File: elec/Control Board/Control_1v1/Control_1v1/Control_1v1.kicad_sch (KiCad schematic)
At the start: 146 parts, among them J1 DB9_Female_MountingHoles, J10 Conn_02x12_Odd_Even, J11 Screw_Terminal_01x02, J14 Conn_01x10, J2 Conn_01x08, J25 Screw_Terminal_01x02, J26 Conn_01x10, J27 Conn_02x12_Odd_Even, J28 Screw_Terminal_01x02, J29 Conn_01x10, J3 Conn_01x08, J37 Conn_01x04_Pin, J4 Conn_01x08, J5 Conn_01x08, J6 Conn_01x08, J7 Conn_01x10, J8 Conn_02x18_Odd_Even, J9 Conn_01x10, Q601 BSS138

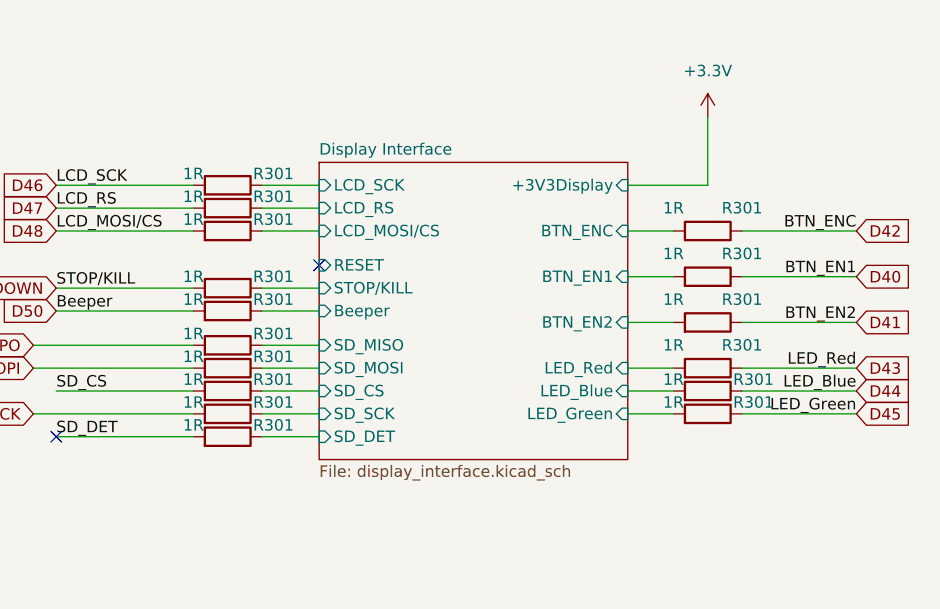
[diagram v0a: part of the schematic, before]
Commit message: unified 1R and 1R0 references
Signed-off-by: lokimetasmith <lokimail@gmail.com>
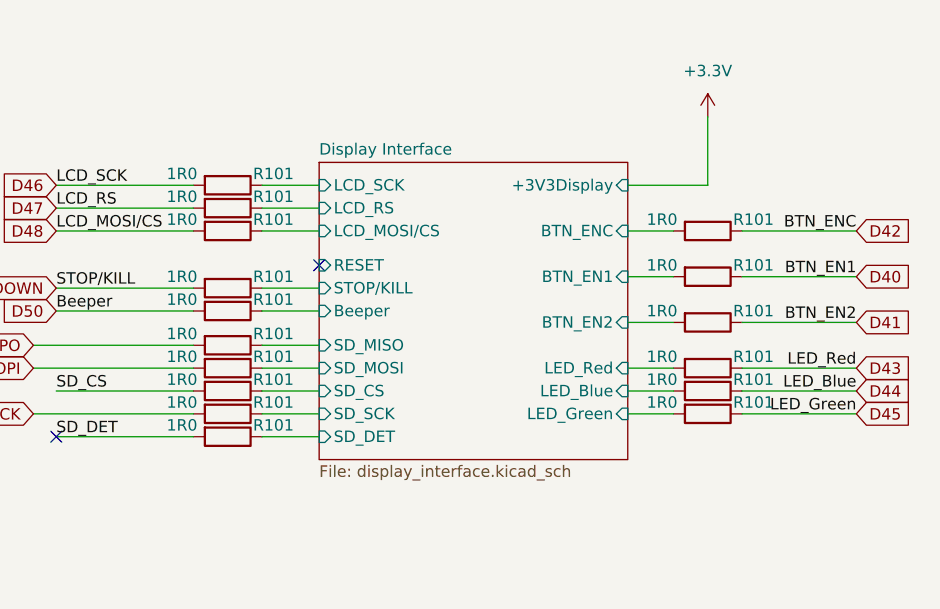
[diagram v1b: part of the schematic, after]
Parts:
- removed R301 (x16): 1R, Resistor_SMD:R_0603_1608Metric_Pad0.98x0.95mm_HandSolder, symbol Device:R
- added R101 (x16): 1R0, Resistor_SMD:R_0603_1608Metric_Pad0.98x0.95mm_HandSolder, symbol Device:R
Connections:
- net CIPO: now also R101.2
- net COPI: now also R101.2
- net D40: now also R101.1
- net D41: now also R101.1
- net D42: now also R101.1
- net D43: now also R101.1
- net D44: now also R101.1
- net D45: now also R101.1
- net D46: now also R101.2
- net D47: now also R101.2
- net D48: now also R101.2
- net D49: now also R101.2
- net D50: now also R101.2
- net Display Interface/BTN_EN1: now also R101.2
- net Display Interface/BTN_EN2: now also R101.2
- net Display Interface/BTN_ENC: now also R101.2
- net Display Interface/Beeper: now also R101.1
- net Display Interface/LCD_MOSI/CS: now also R101.1
- net Display Interface/LCD_RS: now also R101.1
- net Display Interface/LCD_SCK: now also R101.1
- net Display Interface/LED_Blue: now also R101.2
- net Display Interface/LED_Green: now also R101.2
- net Display Interface/LED_Red: now also R101.2
- net Display Interface/SD_CS: now also R101.1
- net Display Interface/SD_DET: now also R101.1
- net Display Interface/SD_MISO: now also R101.1
- net Display Interface/SD_MOSI: now also R101.1
- net Display Interface/SD_SCK: now also R101.1
- net Display Interface/STOP/KILL: now also R101.1
- net SD_CS: now also R101.2
- net SD_DET: now also R101.2
- net SPI_SCK: now also R101.2

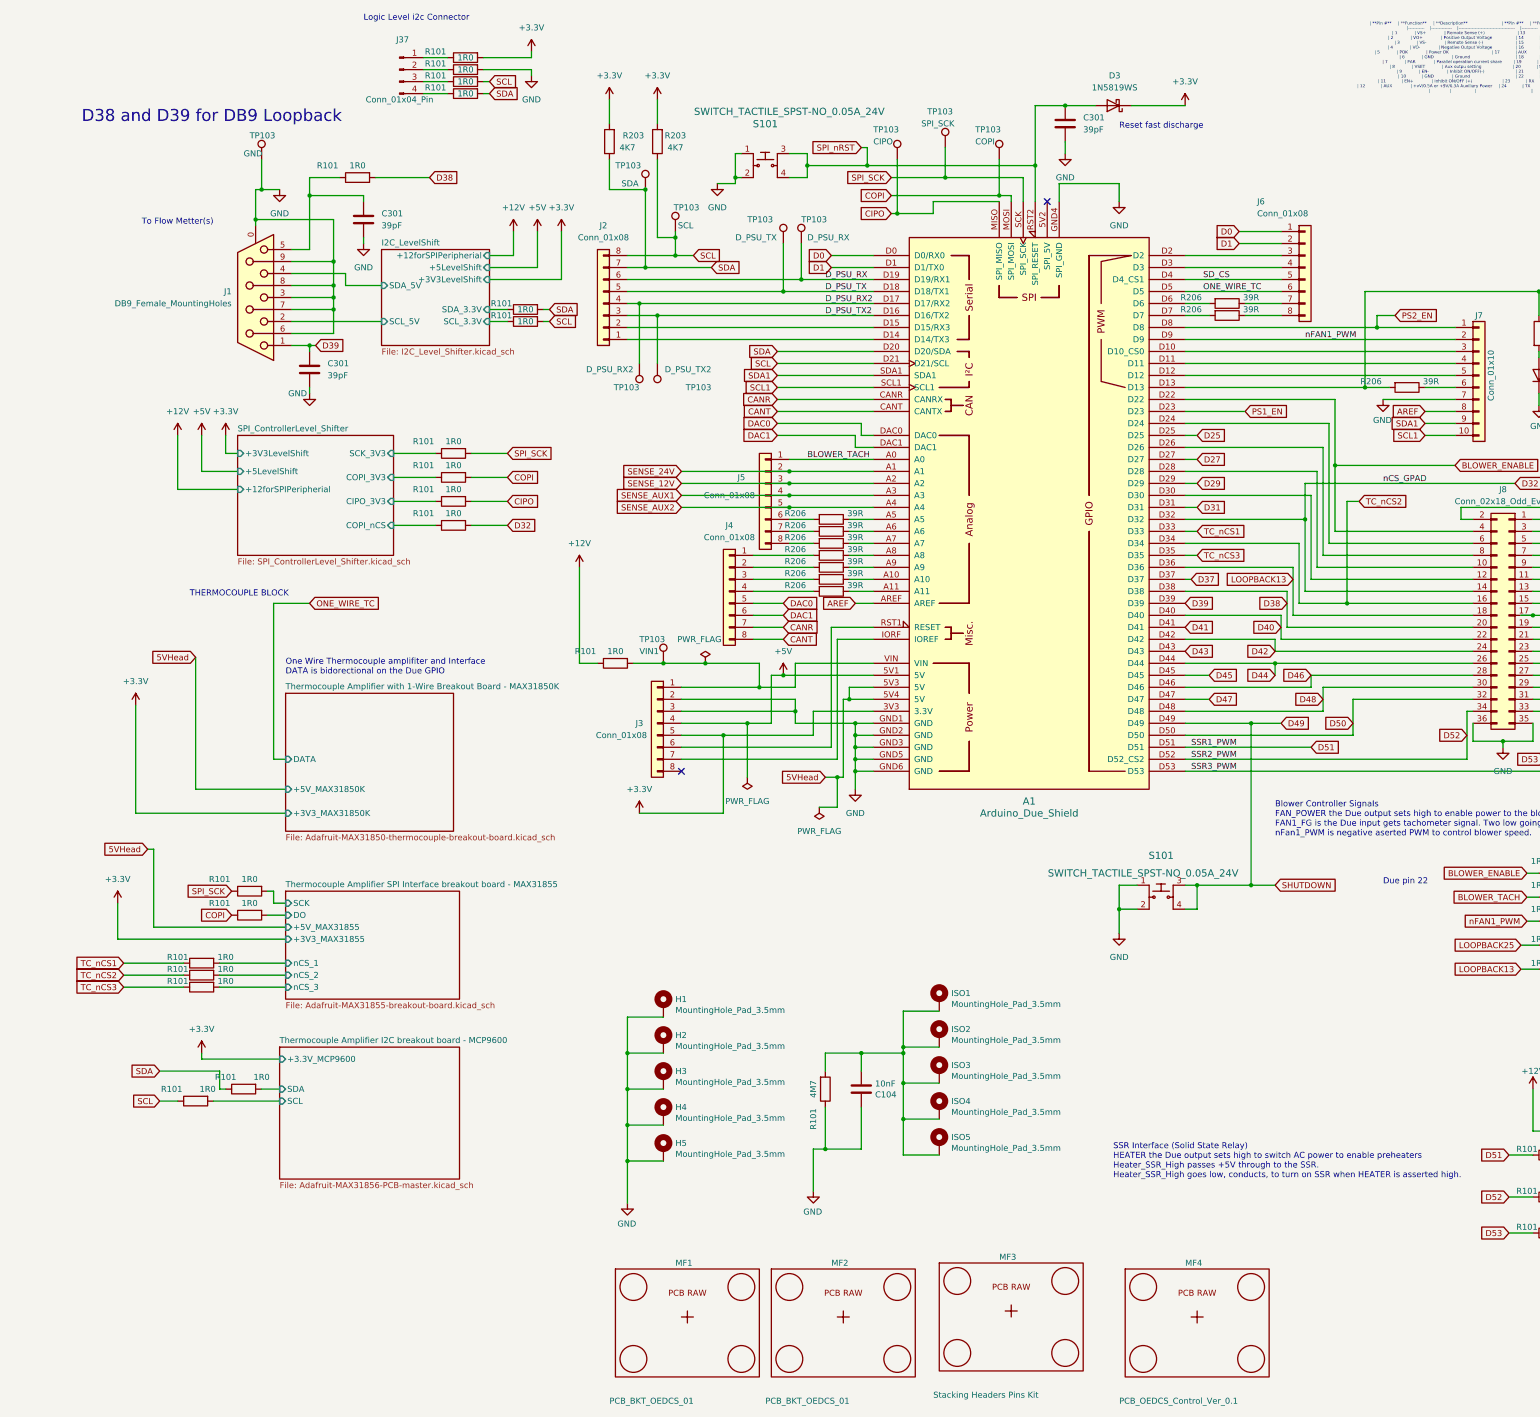
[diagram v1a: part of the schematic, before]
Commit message: reviewed schematic during review with Lee and Lawrence
Design changes include
1 wire disconnect
more interconnect disconnect resistors
switching i2c connector from the i2c bus to i2c_1 bus
confirmed that the board is ready for final layout

Signed-off-by: lokimetasmith <lokimail@gmail.com>
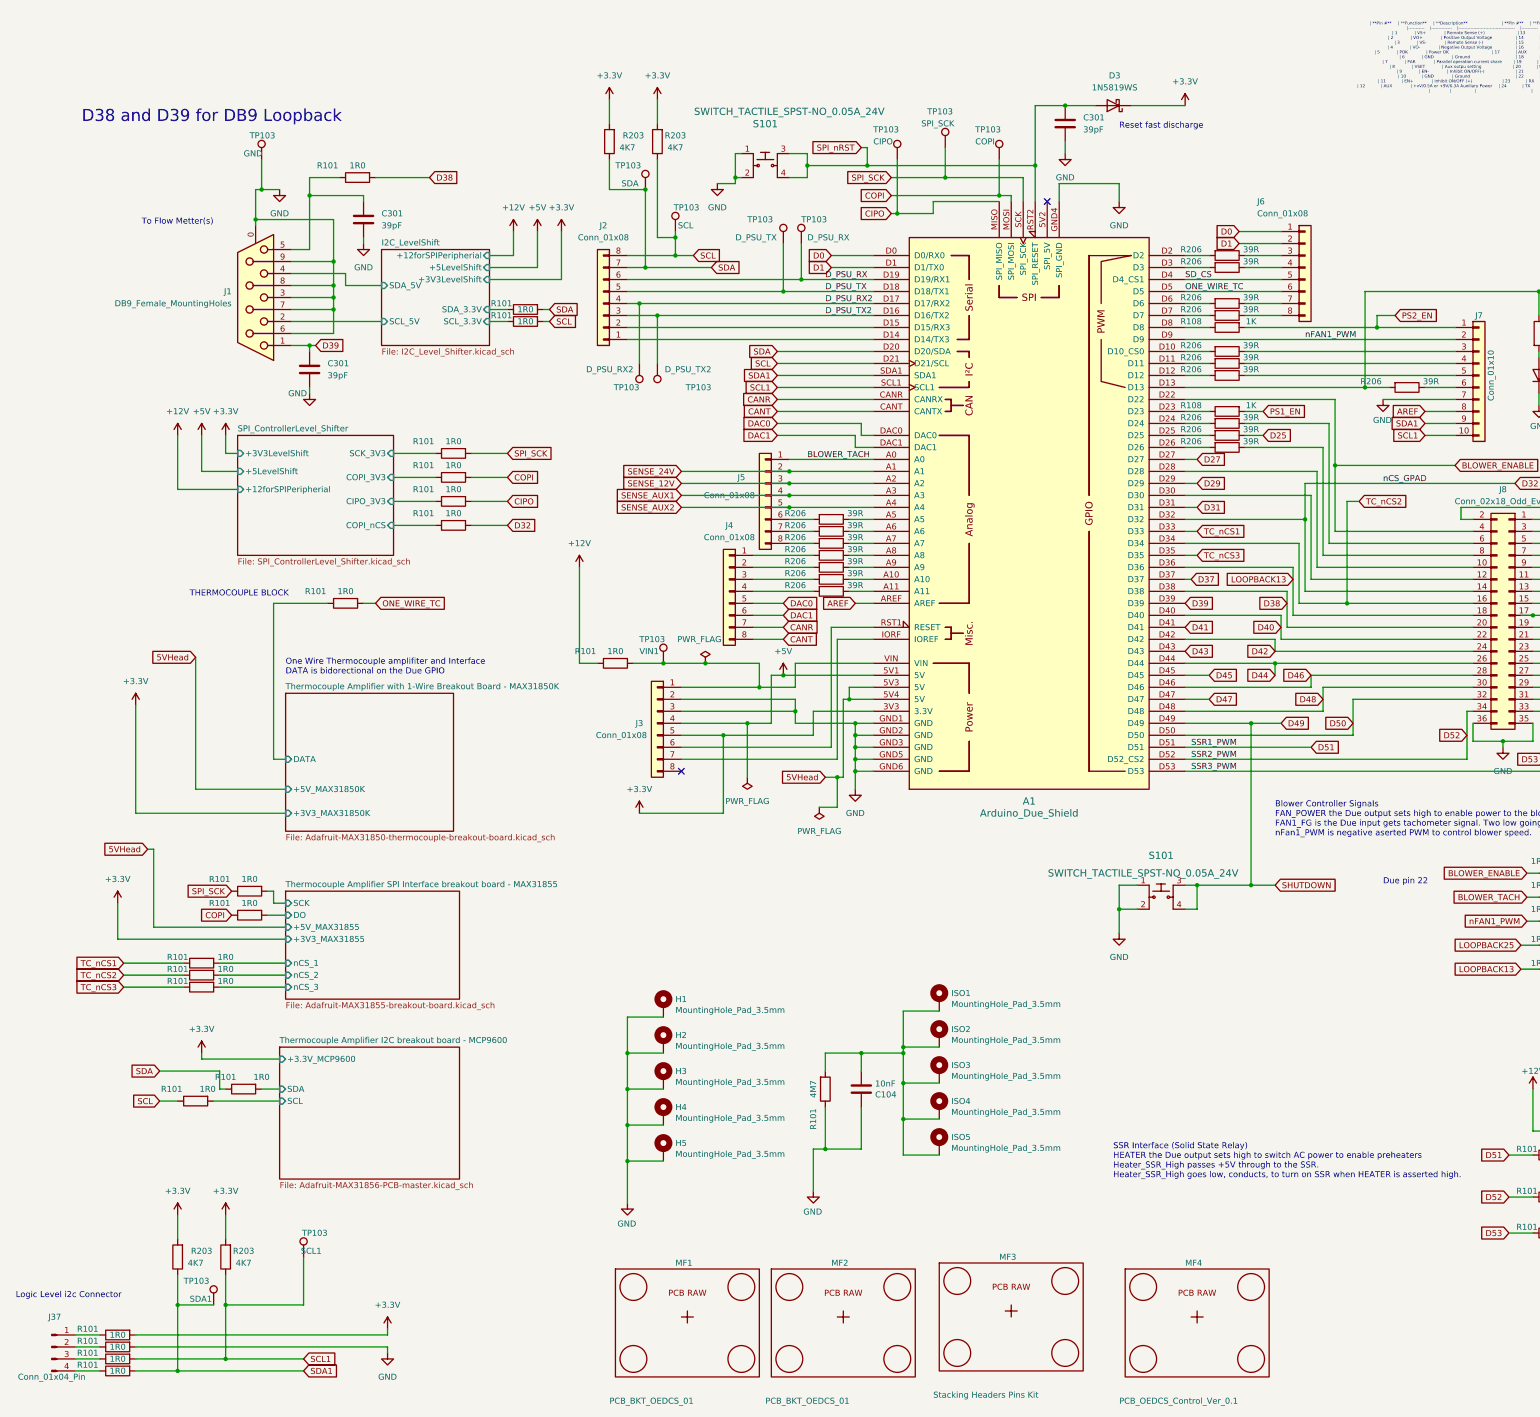
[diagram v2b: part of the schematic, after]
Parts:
- added R101: 1R0, Resistor_SMD:R_0603_1608Metric_Pad0.98x0.95mm_HandSolder, symbol Device:R
- added R108 (x2): 1K, Resistor_SMD:R_0603_1608Metric_Pad0.98x0.95mm_HandSolder, symbol Device:R
- added R203 (x2): 4K7, Resistor_SMD:R_0603_1608Metric_Pad0.98x0.95mm_HandSolder, symbol Device:R
- added R206 (x8): 39R, Resistor_SMD:R_0603_1608Metric_Pad0.98x0.95mm_HandSolder, symbol Device:R
- added TP103: SDA1, TestPoint:TestPoint_Loop_D2.54mm_Drill1.5mm_Beaded, symbol Connector:TestPoint
- added TP103: SCL1, TestPoint:TestPoint_Loop_D2.54mm_Drill1.5mm_Beaded, symbol Connector:TestPoint
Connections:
- net +3.3V: now also R203.2, R203.2
- net D25: now also R206.1; no longer A1.D25
- net ONE_WIRE_TC: now also R101.2
- net PS1_EN: now also R108.2; no longer A1.D23
- net PS2_EN: now also R108.2; no longer A1.D8
- net SCL: no longer R101.2
- net SCL1: now also R101.2, R203.1, TP103.1
- net SDA: no longer R101.2
- net SDA1: now also R101.2, R203.1, TP103.1
- net at J8.6 (Pin_6): now also R206.1; no longer A1.D24
- net at J8.8 (Pin_8): now also R206.1; no longer A1.D26
- net at A1.D10 (D10_CS0): now also R206.2; no longer J7.3 (Pin_3)
- net at A1.D11: now also R206.2; no longer J7.4 (Pin_4)
- net at A1.D12: now also R206.2; no longer J7.5 (Pin_5)
- net at A1.D2: now also R206.2; no longer J6.3 (Pin_3)
- net at J6.4 (Pin_4): now also R206.1; no longer A1.D3
- new net: A1.D25, R206.2
- new net: A1.D3, R206.2
- new net: A1.D24, R206.2
- new net: A1.D23, R108.1
- new net: A1.D26, R206.2
- new net: A1.D8, R108.1
- new net: J6.3 (Pin_3), R206.1
- new net: J7.4 (Pin_4), R206.1
- new net: J7.5 (Pin_5), R206.1
- new net: J7.3 (Pin_3), R206.1
- new net Thermocouple Amplifier with 1-Wire Breakout Board - MAX31850K/DATA: R101.1
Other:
- moved on the sheet: J37, R101

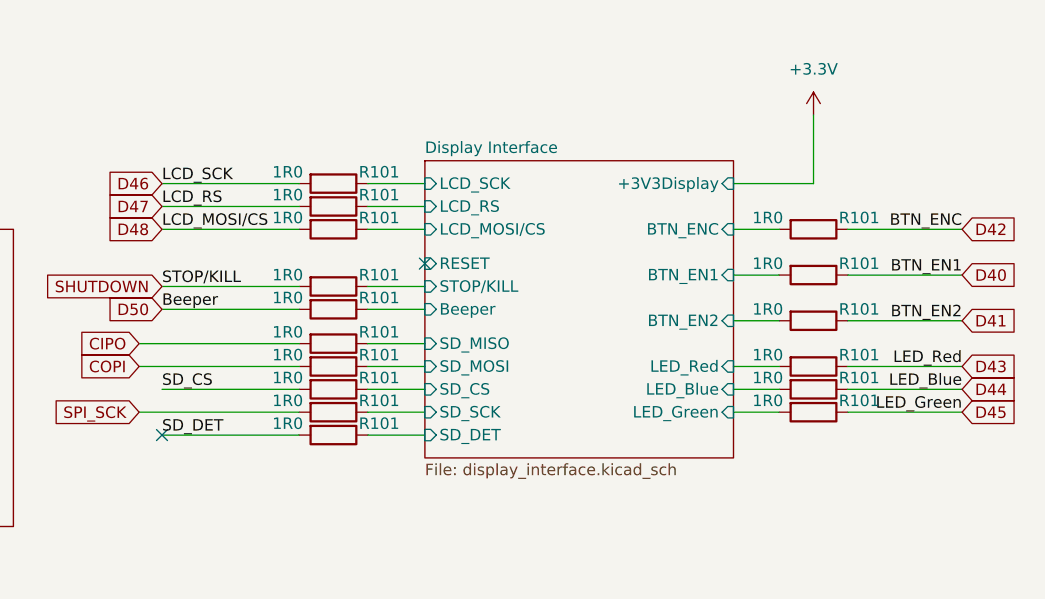
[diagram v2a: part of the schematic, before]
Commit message: Some component placement for display and I2C.
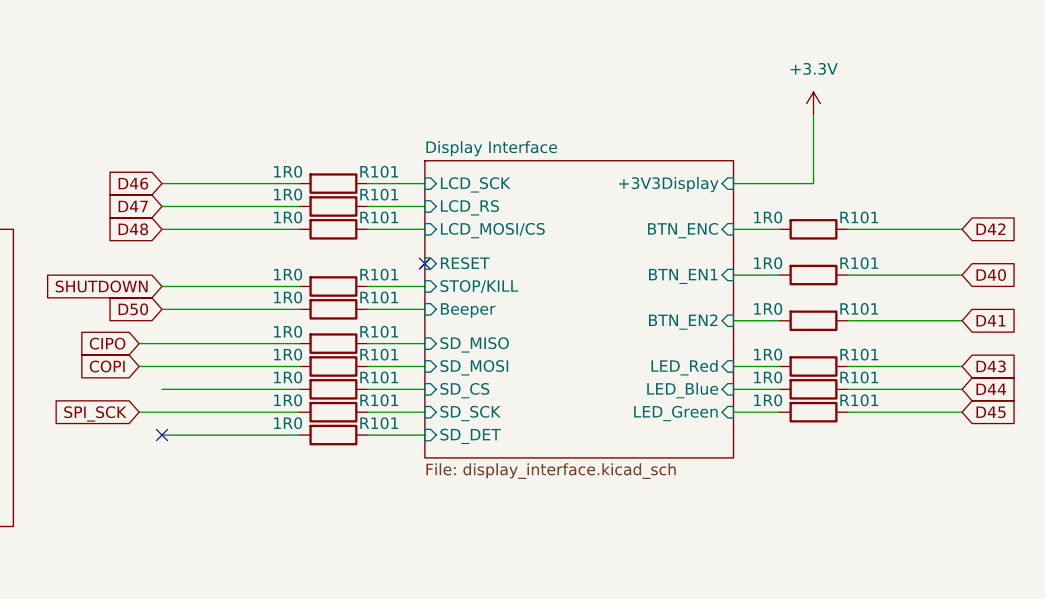
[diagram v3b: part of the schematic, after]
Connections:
- net SD_CS: no longer R101.2
- net SD_DET: no longer names the net of R101.2
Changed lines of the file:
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@@
     (effects (font (size 1.27 1.27)) (justify left bottom))
-  )
-  (label "BTN_EN1" (at 514.35 251.46 180) (fields_autoplaced)
-    (effects (font (size 1.27 1.27)) (justify right bottom))
   )
   (label "SCL" (at 499.11 148.59 180) (fields_autoplaced)
@@
     (effects (font (size 1.27 1.27)) (justify right bottom))
   )
-  (label "BTN_ENC" (at 514.35 246.38 180) (fields_autoplaced)
-    (effects (font (size 1.27 1.27)) (justify right bottom))
-  )
   (label "POK2" (at 461.01 116.84 180) (fields_autoplaced)
     (effects (font (size 1.27 1.27)) (justify right bottom))
@@
     (effects (font (size 1.27 1.27)) (justify right bottom))
   )
-  (label "LCD_RS" (at 425.45 243.84 0) (fields_autoplaced)
-    (effects (font (size 1.27 1.27)) (justify left bottom))
-  )
   (label "SD_CS" (at 283.21 71.12 0) (fields_autoplaced)
     (effects (font (size 1.27 1.27)) (justify left bottom))
@@
     (effects (font (size 1.27 1.27)) (justify right bottom))
   )
-  (label "LCD_SCK" (at 425.45 241.3 0) (fields_autoplaced)
-    (effects (font (size 1.27 1.27)) (justify left bottom))
-  )
   (label "PS_SDA" (at 441.96 63.5 180) (fields_autoplaced)
     (effects (font (size 1.27 1.27)) (justify right bottom))
@@
     (effects (font (size 1.27 1.27)) (justify right bottom))
   )
-  (label "LED_Red" (at 514.35 261.62 180) (fields_autoplaced)
-    (effects (font (size 1.27 1.27)) (justify right bottom))
-  )
-  (label "LED_Green" (at 514.35 266.7 180) (fields_autoplaced)
-    (effects (font (size 1.27 1.27)) (justify right bottom))
-  )
   (label "VS2-" (at 461.01 114.3 180) (fields_autoplaced)
     (effects (font (size 1.27 1.27)) (justify right bottom))
@@
     (effects (font (size 1.27 1.27)) (justify right bottom))
   )
-  (label "BTN_EN2" (at 514.35 256.54 180) (fields_autoplaced)
-    (effects (font (size 1.27 1.27)) (justify right bottom))
-  )
   (label "ACI" (at 461.01 55.88 180) (fields_autoplaced)
     (effects (font (size 1.27 1.27)) (justify right bottom))
@@
     (effects (font (size 1.27 1.27)) (justify right bottom))
   )
-  (label "SD_DET" (at 425.45 269.24 0) (fields_autoplaced)
-    (effects (font (size 1.27 1.27)) (justify left bottom))
-  )
   (label "VO2-" (at 439.42 114.3 180) (fields_autoplaced)
     (effects (font (size 1.27 1.27)) (justify right bottom))
@@
     (effects (font (size 1.27 1.27)) (justify right bottom))
   )
-  (label "LED_Blue" (at 514.35 264.16 180) (fields_autoplaced)
-    (effects (font (size 1.27 1.27)) (justify right bottom))
-  )
   (label "VCI2" (at 461.01 129.54 180) (fields_autoplaced)
     (effects (font (size 1.27 1.27)) (justify right bottom))
@@
     (effects (font (size 1.27 1.27)) (justify left bottom))
   )
-  (label "LCD_MOSI{slash}CS" (at 425.45 246.38 0) (fields_autoplaced)
-    (effects (font (size 1.27 1.27)) (justify left bottom))
-  )
-  (label "SD_CS" (at 425.45 264.16 0) (fields_autoplaced)
-    (effects (font (size 1.27 1.27)) (justify left bottom))
-  )
   (label "GND" (at 439.42 116.84 180) (fields_autoplaced)
     (effects (font (size 1.27 1.27)) (justify right bottom))
@@
     (effects (font (size 1.27 1.27)) (justify left bottom))
   )
-  (label "Beeper" (at 425.45 255.27 0) (fields_autoplaced)
-    (effects (font (size 1.27 1.27)) (justify left bottom))
-  )
   (label "PS2_SDA" (at 441.96 134.62 180) (fields_autoplaced)
     (effects (font (size 1.27 1.27)) (justify right bottom))
@@
     (effects (font (size 1.27 1.27)) (justify right bottom))
   )
-  (label "STOP{slash}KILL" (at 425.45 252.73 0) (fields_autoplaced)
-    (effects (font (size 1.27 1.27)) (justify left bottom))
-  )
   (label "GND" (at 439.42 55.88 180) (fields_autoplaced)
